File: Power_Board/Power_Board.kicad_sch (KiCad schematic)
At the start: 20 parts, among them J1 Conn_01x10_Female, J2 Conn_01x10_Female, J3 Conn_01x06_Female, J4 Screw_Terminal_01x02, J5 Screw_Terminal_01x02

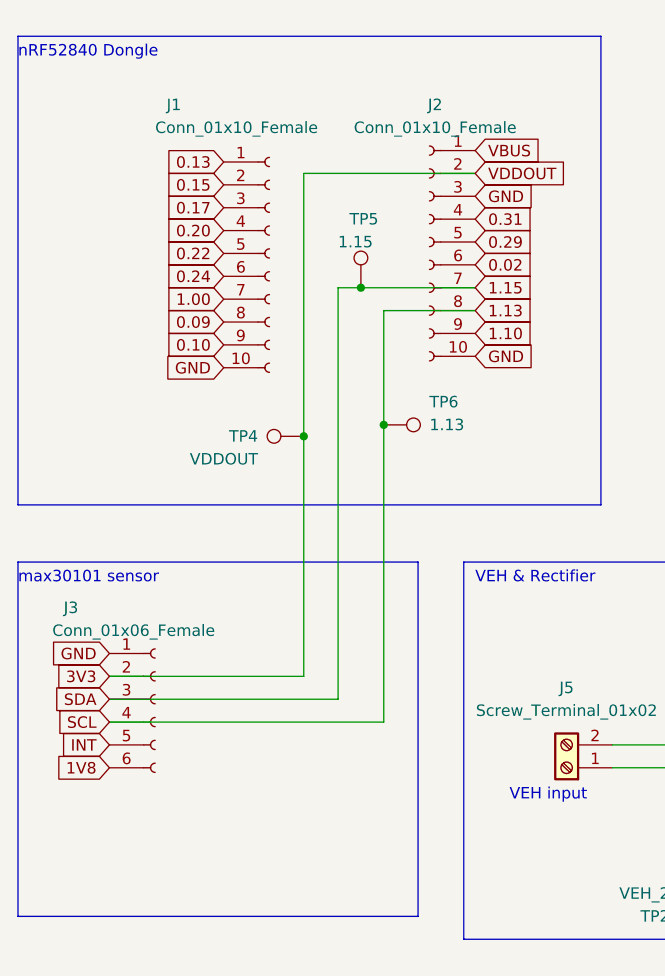
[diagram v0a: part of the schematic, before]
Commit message: Removed sensor from board
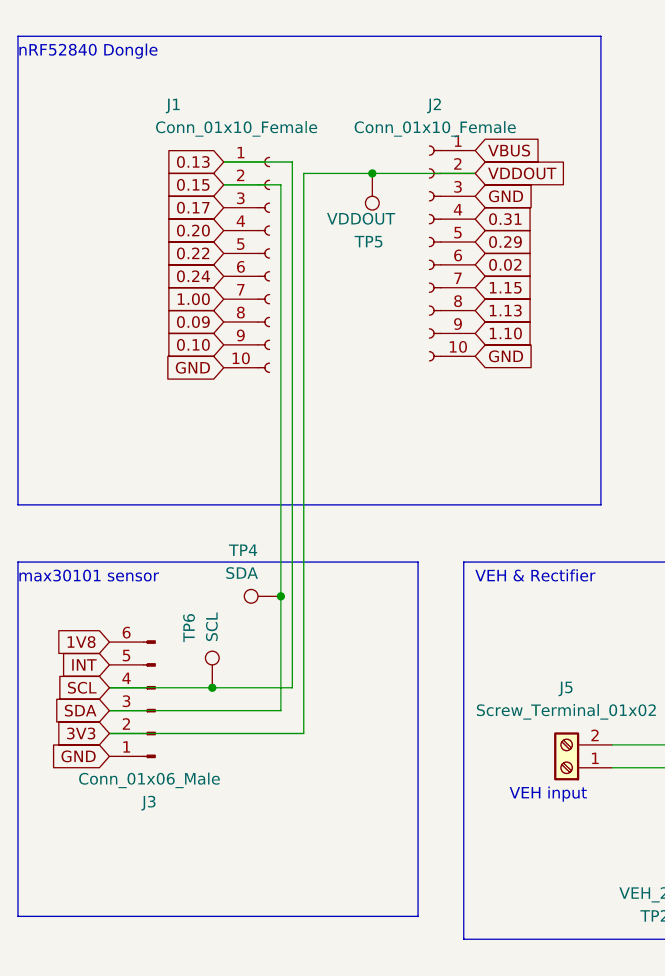
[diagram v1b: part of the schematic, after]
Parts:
- removed J3: Conn_01x06_Female, Connector_PinSocket_2.54mm:PinSocket_1x06_P2.54mm_Vertical, symbol Connector:Conn_01x06_Female
- added J3: Conn_01x06_Male, symbol Connector:Conn_01x06_Male
- H1: footprint (none) -> MountingHole:MountingHole_2.2mm_M2
- TP4: value VDDOUT -> SDA
- TP5: value 1.15 -> VDDOUT
- TP6: value 1.13 -> SCL
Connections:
- net 0.13: now also TP6.1, J3.4 (Pin_4)
- net 0.15: now also TP4.1, J3.3 (Pin_3)
- net 1.13: no longer TP6.1
- net 1.15: no longer TP5.1
- net 1V8: now also J3.6 (Pin_6)
- net 3V3: now also TP5.1, J3.2 (Pin_2); no longer TP4.1
- net GND: now also J3.1 (Pin_1)
- net INT: now also J3.5 (Pin_5)
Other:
- moved on the sheet: TP4, TP5, TP6

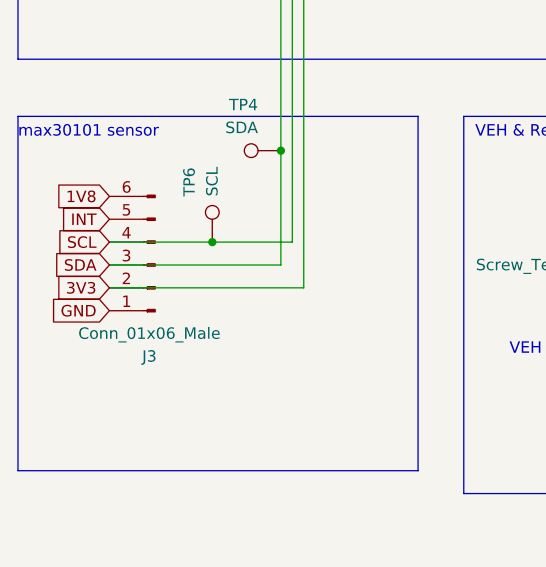
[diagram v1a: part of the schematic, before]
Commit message: new pcb layout
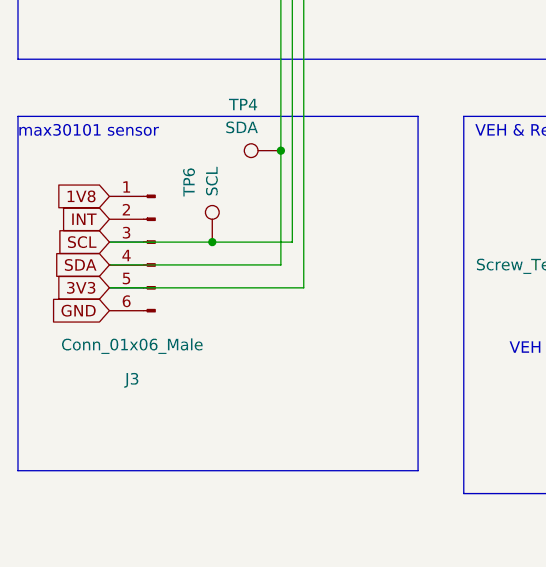
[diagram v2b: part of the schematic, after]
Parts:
- J3: footprint (none) -> Connector_PinHeader_2.54mm:PinHeader_1x06_P2.54mm_Horizontal
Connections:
- net 0.13: now also J3.3 (Pin_3); no longer J3.4 (Pin_4)
- net 0.15: now also J3.4 (Pin_4); no longer J3.3 (Pin_3)
- net 1V8: now also J3.1 (Pin_1); no longer J3.6 (Pin_6)
- net 3V3: now also J3.5 (Pin_5); no longer J3.2 (Pin_2)
- net GND: now also J3.6 (Pin_6); no longer J3.1 (Pin_1)
- net INT: now also J3.2 (Pin_2); no longer J3.5 (Pin_5)
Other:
- moved on the sheet: J3
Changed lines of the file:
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@@
     (pin "1")
   )
-  (symbol (lib_id "Connector:Conn_01x06_Male") (at 41.91 93.98 180) (unit 1)
+  (symbol (lib_id "Connector:Conn_01x06_Male") (at 41.91 91.44 0) (mirror y) (unit 1)
     (in_bom yes) (on_board yes)
-    (property "Reference" "J3" (id 0) (at 41.275 104.14 0))
-    (property "Value" "Conn_01x06_Male" (id 1) (at 41.275 101.6 0))
-    (property "Footprint" "" (id 2) (at 41.91 93.98 0)
+    (property "Reference" "J3" (id 0) (at 39.37 106.68 0))
+    (property "Value" "Conn_01x06_Male" (id 1) (at 39.37 102.87 0))
+    (property "Footprint" "Connector_PinHeader_2.54mm:PinHeader_1x06_P2.54mm_Horizontal" (id 2) (at 41.91 91.44 0)
       (effects (font (size 1.27 1.27)) hide)
     )
-    (property "Datasheet" "~" (id 3) (at 41.91 93.98 0)
+    (property "Datasheet" "~" (id 3) (at 41.91 91.44 0)
       (effects (font (size 1.27 1.27)) hide)
     )

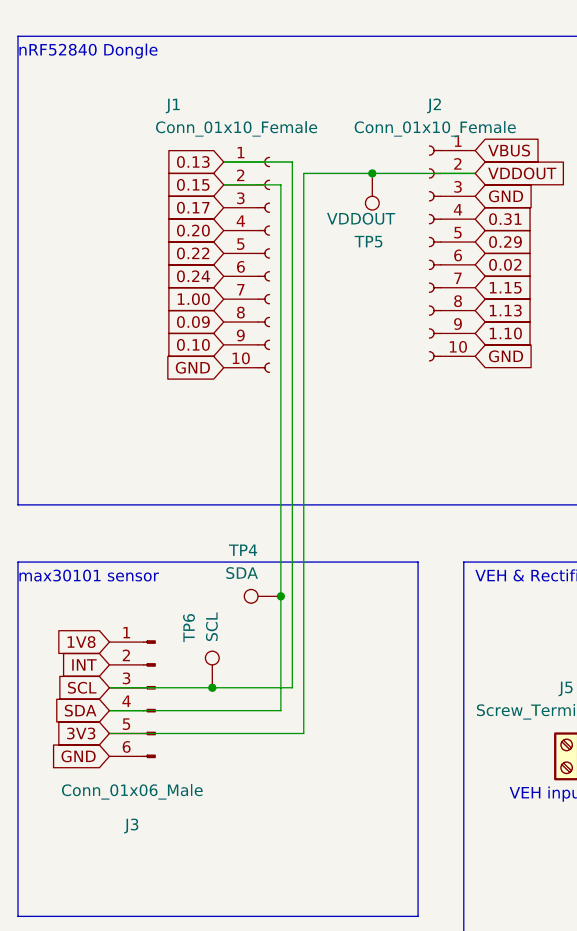
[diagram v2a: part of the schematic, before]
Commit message: Added GND plane and rerouted
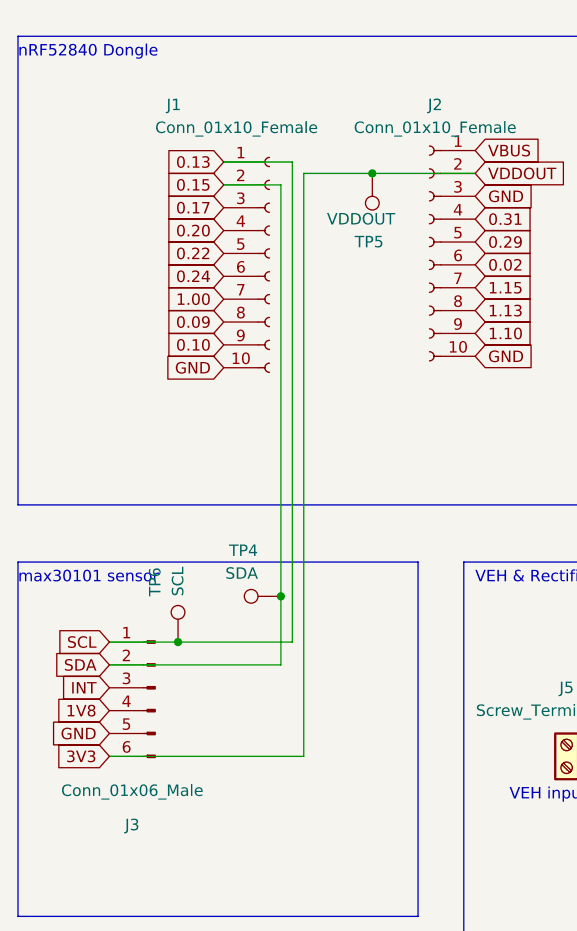
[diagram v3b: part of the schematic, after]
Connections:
- net 0.13: now also J3.1 (Pin_1); no longer J3.3 (Pin_3)
- net 0.15: now also J3.2 (Pin_2); no longer J3.4 (Pin_4)
- net 1V8: now also J3.4 (Pin_4); no longer J3.1 (Pin_1)
- net 3V3: now also J3.6 (Pin_6); no longer J3.5 (Pin_5)
- net GND: now also J3.5 (Pin_5); no longer J3.6 (Pin_6)
- net INT: now also J3.3 (Pin_3); no longer J3.2 (Pin_2)
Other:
- moved on the sheet: TP6

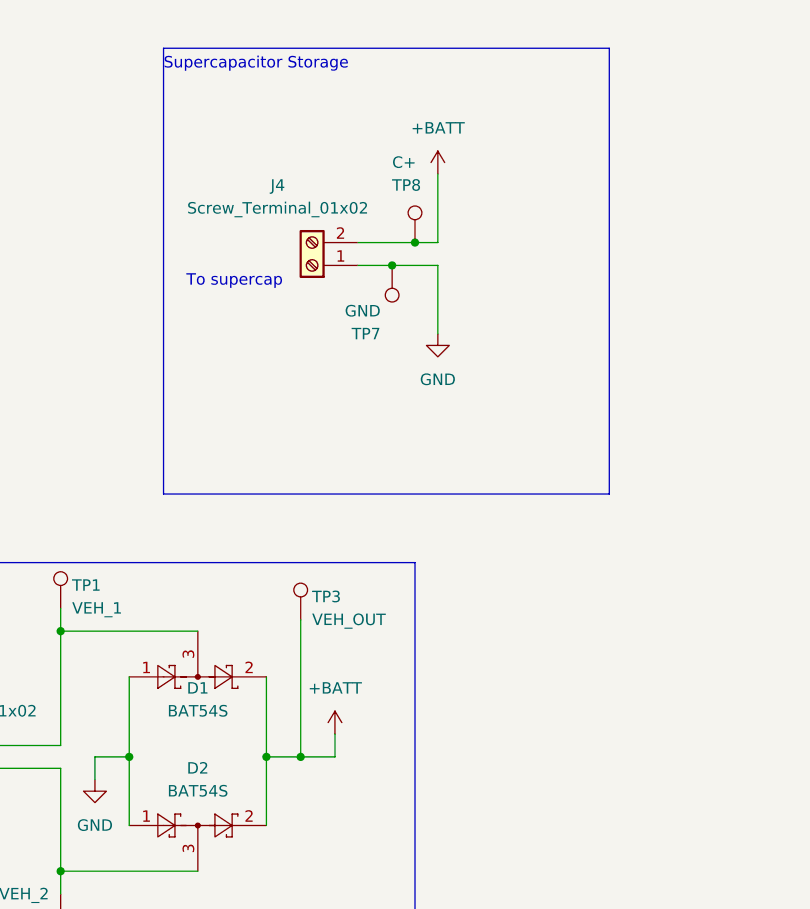
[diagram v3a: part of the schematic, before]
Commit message: Added off switch(jumper)
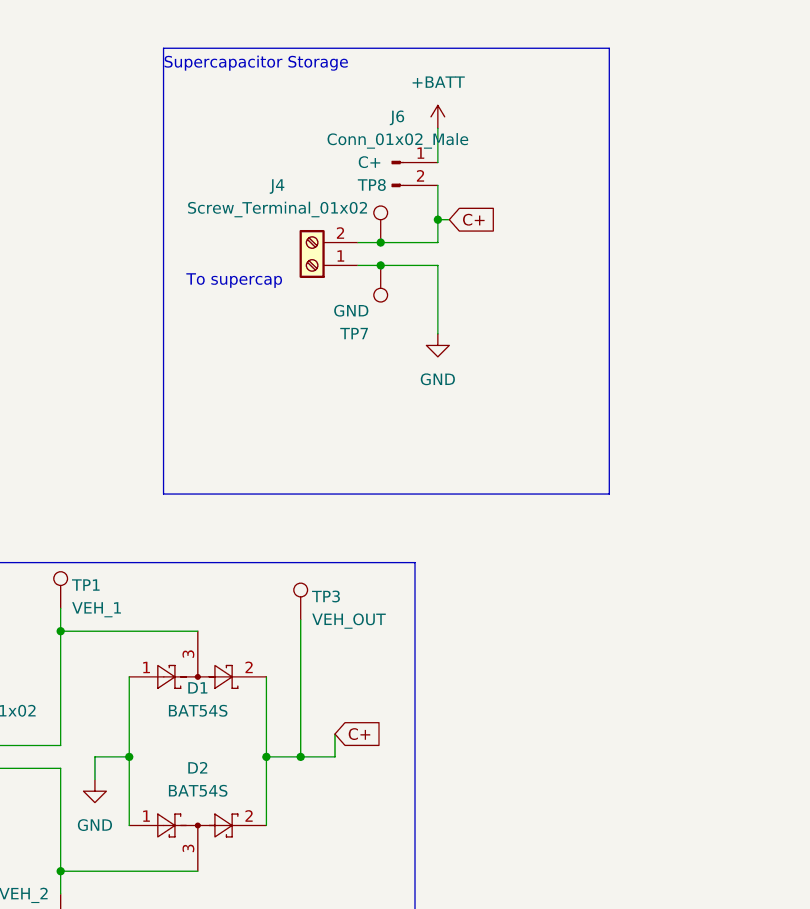
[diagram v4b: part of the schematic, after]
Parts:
- added J6: Conn_01x02_Male, symbol Connector:Conn_01x02_Male
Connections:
- net +BATT: now also J6.1 (Pin_1); no longer D1.2, D2.2, J4.2 (Pin_2), TP3.1, TP8.1
- new net C+: D1.2, D2.2, J4.2 (Pin_2), J6.2 (Pin_2), TP3.1, TP8.1
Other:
- moved on the sheet: TP7, TP8
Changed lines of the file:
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@@
     (company "KTH")
   )
-  (junction (at 139.7 41.91) (diameter 0) (color 0 0 0 0)
-  )
   (junction (at 66.04 34.29) (diameter 0) (color 0 0 0 0)
   )
-  (junction (at 137.16 44.45) (diameter 0) (color 0 0 0 0)
+  (junction (at 135.89 41.91) (diameter 0) (color 0 0 0 0)
+  )
+  (junction (at 135.89 44.45) (diameter 0) (color 0 0 0 0)
+  )
+  (junction (at 142.24 39.37) (diameter 0) (color 0 0 0 0)
   )
   (junction (at 55.88 81.28) (diameter 0) (color 0 0 0 0)
@@
     (stroke (width 0) (type default) (color 0 0 0 0))
   )
-  (wire (pts (xy 137.16 44.45) (xy 142.24 44.45))
+  (wire (pts (xy 142.24 35.56) (xy 142.24 39.37))
     (stroke (width 0) (type default) (color 0 0 0 0))
   )
@@
     (stroke (width 0) (type default) (color 0 0 0 0))
   )
+  (wire (pts (xy 135.89 44.45) (xy 142.24 44.45))
+    (stroke (width 0) (type default) (color 0 0 0 0))
+  )
   (polyline (pts (xy 284.48 115.57) (xy 284.48 148.59))
     (stroke (width 0) (type default) (color 0 0 0 0))
@@
     (stroke (width 0) (type default) (color 0 0 0 0))
   )
-  (wire (pts (xy 142.24 34.29) (xy 142.24 41.91))
-    (stroke (width 0) (type default) (color 0 0 0 0))
-  )
   (wire (pts (xy 100.33 82.55) (xy 100.33 85.09))
     (stroke (width 0) (type default) (color 0 0 0 0))
@@
     (stroke (width 0) (type default) (color 0 0 0 0))
   )
+  (wire (pts (xy 133.35 41.91) (xy 135.89 41.91))
+    (stroke (width 0) (type default) (color 0 0 0 0))
+  )
   (wire (pts (xy 123.19 99.06) (xy 127 99.06))
     (stroke (width 0) (type default) (color 0 0 0 0))
@@
     (stroke (width 0) (type default) (color 0 0 0 0))
   )
-  (wire (pts (xy 133.35 41.91) (xy 139.7 41.91))
-    (stroke (width 0) (type default) (color 0 0 0 0))
-  )
   (polyline (pts (xy 254 148.59) (xy 231.14 148.59))
     (stroke (width 0) (type default) (color 0 0 0 0))
@@
     (stroke (width 0) (type default) (color 0 0 0 0))
   )
-  (wire (pts (xy 133.35 44.45) (xy 137.16 44.45))
+  (wire (pts (xy 133.35 44.45) (xy 135.89 44.45))
     (stroke (width 0) (type default) (color 0 0 0 0))
   )
@@
     (stroke (width 0) (type default) (color 0 0 0 0))
   )
+  (wire (pts (xy 142.24 29.21) (xy 142.24 33.02))
+    (stroke (width 0) (type default) (color 0 0 0 0))
+  )
   (polyline (pts (xy 257.81 110.49) (xy 284.48 110.49))
     (stroke (width 0) (type default) (color 0 0 0 0))
@@
     (stroke (width 0) (type default) (color 0 0 0 0))
   )
+  (wire (pts (xy 142.24 39.37) (xy 142.24 41.91))
+    (stroke (width 0) (type default) (color 0 0 0 0))
+  )
   (polyline (pts (xy 257.81 148.59) (xy 257.81 110.49))
     (stroke (width 0) (type default) (color 0 0 0 0))
@@
     (stroke (width 0) (type default) (color 0 0 0 0))
   )
+  (wire (pts (xy 142.24 39.37) (xy 143.51 39.37))
+    (stroke (width 0) (type default) (color 0 0 0 0))
+  )
   (wire (pts (xy 36.83 88.9) (xy 55.88 88.9))
     (stroke (width 0) (type default) (color 0 0 0 0))
@@
     (stroke (width 0) (type default) (color 0 0 0 0))
   )
-  (wire (pts (xy 139.7 41.91) (xy 142.24 41.91))
-    (stroke (width 0) (type default) (color 0 0 0 0))
-  )
   (wire (pts (xy 100.33 111.76) (xy 100.33 114.3))
     (stroke (width 0) (type default) (color 0 0 0 0))
@@
   )
   (wire (pts (xy 127 83.82) (xy 127 99.06))
+    (stroke (width 0) (type default) (color 0 0 0 0))
+  )
+  (wire (pts (xy 135.89 41.91) (xy 142.24 41.91))
     (stroke (width 0) (type default) (color 0 0 0 0))
   )
@@
     )
   )
+  (global_label "C+" (shape input) (at 143.51 39.37 0) (fields_autoplaced)
+    (effects (font (size 1.27 1.27)) (justify left))
+    (property "Intersheet References" "${INTERSHEET_REFS}" (id 0) (at 148.7655 39.2906 0)
+      (effects (font (size 1.27 1.27)) (justify left) hide)
+    )
+  )
   (global_label "INT" (shape input) (at 36.83 91.44 180) (fields_autoplaced)
     (effects (font (size 1.27 1.27)) (justify right))
@@
     (property "Intersheet References" "${INTERSHEET_REFS}" (id 0) (at 43.2464 55.8006 0)
       (effects (font (size 1.27 1.27)) (justify right) hide)
+    )
+  )
+  (global_label "C+" (shape input) (at 130.81 96.52 0) (fields_autoplaced)
+    (effects (font (size 1.27 1.27)) (justify left))
+    (property "Intersheet References" "${INTERSHEET_REFS}" (id 0) (at 136.0655 96.4406 0)
+      (effects (font (size 1.27 1.27)) (justify left) hide)
     )
   )
@@
     (pin "2")
   )
-  (symbol (lib_id "power:+BATT") (at 142.24 34.29 0) (unit 1)
-    (in_bom yes) (on_board yes) (fields_autoplaced)
-    (property "Reference" "#PWR0108" (id 0) (at 142.24 38.1 0)
-      (effects (font (size 1.27 1.27)) hide)
-    )
-    (property "Value" "+BATT" (id 1) (at 142.24 29.21 0))
-    (property "Footprint" "" (id 2) (at 142.24 34.29 0)
-      (effects (font (size 1.27 1.27)) hide)
-    )
-    (property "Datasheet" "" (id 3) (at 142.24 34.29 0)
+  (symbol (lib_id "power:+BATT") (at 142.24 29.21 0) (unit 1)
+    (in_bom yes) (on_board yes) (fields_autoplaced)
+    (property "Reference" "#PWR0108" (id 0) (at 142.24 33.02 0)
+      (effects (font (size 1.27 1.27)) hide)
+    )
+    (property "Value" "+BATT" (id 1) (at 142.24 24.13 0))
+    (property "Footprint" "" (id 2) (at 142.24 29.21 0)
+      (effects (font (size 1.27 1.27)) hide)
+    )
+    (property "Datasheet" "" (id 3) (at 142.24 29.21 0)
       (effects (font (size 1.27 1.27)) hide)
     )
@@
     (pin "1")
   )
-  (symbol (lib_id "power:+BATT") (at 130.81 96.52 0) (unit 1)
-    (in_bom yes) (on_board yes) (fields_autoplaced)
-    (property "Reference" "#PWR0106" (id 0) (at 130.81 100.33 0)
-      (effects (font (size 1.27 1.27)) hide)
-    )
-    (property "Value" "+BATT" (id 1) (at 130.81 91.44 0))
-    (property "Footprint" "" (id 2) (at 130.81 96.52 0)
-      (effects (font (size 1.27 1.27)) hide)
-    )
-    (property "Datasheet" "" (id 3) (at 130.81 96.52 0)
-      (effects (font (size 1.27 1.27)) hide)
-    )
-    (pin "1")
-  )
-  (symbol (lib_id "Connector:TestPoint") (at 137.16 44.45 180) (unit 1)
-    (in_bom yes) (on_board yes)
-    (property "Reference" "TP7" (id 0) (at 135.89 52.07 0)
-      (effects (font (size 1.27 1.27)) (justify left))
-    )
-    (property "Value" "GND" (id 1) (at 135.89 49.53 0)
-      (effects (font (size 1.27 1.27)) (justify left))
-    )
-    (property "Footprint" "TestPoint:TestPoint_Pad_D1.5mm" (id 2) (at 132.08 44.45 0)
-      (effects (font (size 1.27 1.27)) hide)
-    )
-    (property "Datasheet" "~" (id 3) (at 132.08 44.45 0)
-      (effects (font (size 1.27 1.27)) hide)
-    )
-    (pin "1")
-  )
-  (symbol (lib_id "Connector:TestPoint") (at 139.7 41.91 0) (unit 1)
-    (in_bom yes) (on_board yes)
-    (property "Reference" "TP8" (id 0) (at 137.16 35.56 0)
-      (effects (font (size 1.27 1.27)) (justify left))
-    )
-    (property "Value" "C+" (id 1) (at 137.16 33.02 0)
-      (effects (font (size 1.27 1.27)) (justify left))
-    )
-    (property "Footprint" "TestPoint:TestPoint_Pad_D1.5mm" (id 2) (at 144.78 41.91 0)
-      (effects (font (size 1.27 1.27)) hide)
-    )
-    (property "Datasheet" "~" (id 3) (at 144.78 41.91 0)
+  (symbol (lib_id "Connector:TestPoint") (at 135.89 44.45 180) (unit 1)
+    (in_bom yes) (on_board yes)
+    (property "Reference" "TP7" (id 0) (at 134.62 52.07 0)
+      (effects (font (size 1.27 1.27)) (justify left))
+    )
+    (property "Value" "GND" (id 1) (at 134.62 49.53 0)
+      (effects (font (size 1.27 1.27)) (justify left))
+    )
+    (property "Footprint" "TestPoint:TestPoint_Pad_D1.5mm" (id 2) (at 130.81 44.45 0)
+      (effects (font (size 1.27 1.27)) hide)
+    )
+    (property "Datasheet" "~" (id 3) (at 130.81 44.45 0)
+      (effects (font (size 1.27 1.27)) hide)
+    )
+    (pin "1")
+  )
+  (symbol (lib_id "Connector:TestPoint") (at 135.89 41.91 0) (unit 1)
+    (in_bom yes) (on_board yes)
+    (property "Reference" "TP8" (id 0) (at 133.35 35.56 0)
+      (effects (font (size 1.27 1.27)) (justify left))
+    )
+    (property "Value" "C+" (id 1) (at 133.35 33.02 0)
+      (effects (font (size 1.27 1.27)) (justify left))
+    )
+    (property "Footprint" "TestPoint:TestPoint_Pad_D1.5mm" (id 2) (at 140.97 41.91 0)
+      (effects (font (size 1.27 1.27)) hide)
+    )
+    (property "Datasheet" "~" (id 3) (at 140.97 41.91 0)
       (effects (font (size 1.27 1.27)) hide)
     )
@@
     (pin "9")
   )
+  (symbol (lib_id "Connector:Conn_01x02_Male") (at 137.16 33.02 0) (unit 1)
+    (in_bom yes) (on_board yes) (fields_autoplaced)
+    (property "Reference" "J6" (id 0) (at 137.795 27.94 0))
+    (property "Value" "Conn_01x02_Male" (id 1) (at 137.795 30.48 0))
+    (property "Footprint" "" (id 2) (at 137.16 33.02 0)
+      (effects (font (size 1.27 1.27)) hide)
+    )
+    (property "Datasheet" "~" (id 3) (at 137.16 33.02 0)
+      (effects (font (size 1.27 1.27)) hide)
+    )
+    (pin "1")
+    (pin "2")
+  )
   (sheet_instances
     (path "/" (page "1"))
@@
       (reference "#PWR0105") (unit 1) (value "+BATT") (footprint "")
     )
-    (path "/44a31b42-c551-47f3-95bb-1cbc821cc480"
-      (reference "#PWR0106") (unit 1) (value "+BATT") (footprint "")
-    )
     (path "/b6be9306-984d-4d54-acbc-5e0cac1822df"
       (reference "#PWR0107") (unit 1) (value "GND") (footprint "")
@@
       (reference "J5") (unit 1) (value "Screw_Terminal_01x02") (footprint "TerminalBlock_RND:TerminalBlock_RND_205-00001_1x02_P5.00mm_Horizontal")
     )
+    (path "/fb3637d4-9e53-4e33-8fdd-4487b22e66d8"
+      (reference "J6") (unit 1) (value "Conn_01x02_Male") (footprint "Connector_PinHeader_2.54mm:PinHeader_1x02_P2.54mm_Vertical")
+    )
     (path "/0b336ad3-e31a-4a32-8667-1758901ab866"
